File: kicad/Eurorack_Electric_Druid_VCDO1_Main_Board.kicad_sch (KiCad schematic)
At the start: 97 parts, among them J3 EuroPower_JST_3P, J4 EURO_PWR_16P, Q1 2N3904, U1 78M05, U2 79M05, U3 VCDO1, U4 TL074, U5 TL072, U6 TL074, U7 TL072

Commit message: updated schematic rev0.1.3
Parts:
- removed U7: TL072, DIYSynthMNL:DIP-8_W7.62mm_LongPads, symbol Amplifier_Operational:TL072
- added R51 (x4): 100K, DIYSynthMNL:R_quarter_watt_L6.3mm_D2.5mm_P7.62mm, symbol Device:R
- added U2: TL074, symbol Amplifier_Operational:TL074
- added unit 5 of U2
- added unit 4 of U2
- added unit 3 of U2
- added unit 2 of U2
- D16: value (none) -> ~
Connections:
- net +12V: now also U2.4 (V+)
- net +5V: now also Q1.3 (C); no longer R22.1
- net -12V: now also U2.11 (V-)
- net DIN_Glide_Input: now also Q1.1 (E), R22.1; no longer Q1.3 (C), R22.2
- net GND: now also R22.2, U2.10 (+), U2.12 (+), U2.3 (+), U2.5 (+); no longer Q1.1 (E)
- net at R50.2, R51.1, R53.2: now also U2.2 (-)
- net at R51.2: now also R51.1, U2.1; no longer R52.1
- net at R46.2, R47.1, R49.2: now also U2.9 (-)
- net at R48.1: now also R51.2, U2.14; no longer R47.2
- new net: R51.1, R51.2, U2.6 (-)
- new net: R51.2, R52.1, U2.7
- new net: R51.1, R51.2, U2.13 (-)
- new net: R47.2, R51.1, U2.8
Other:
- title: Eurorack Electric Druid VCDO1 - Main Board -> Eurorack Electric Druid VCDO1 - Control Board
- moved on the sheet: D13, D14, D15, D16, R21, R22, R46, R47, R48, R49, R52

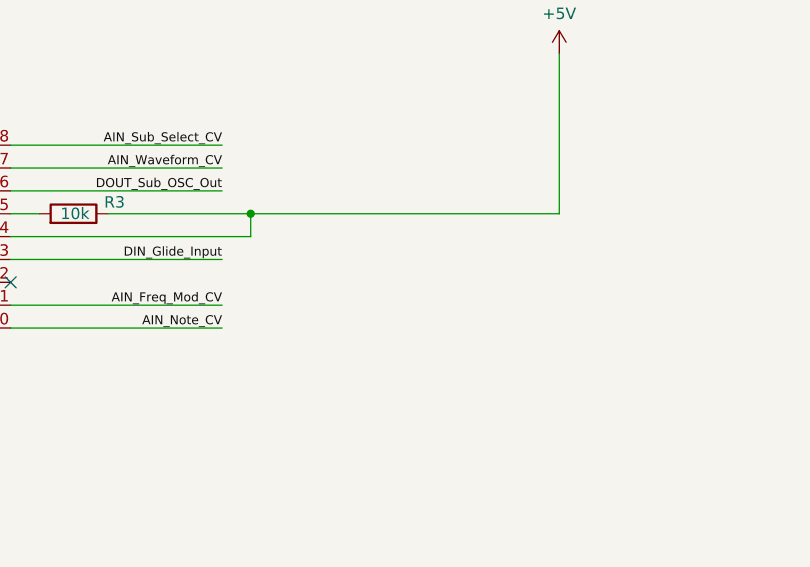
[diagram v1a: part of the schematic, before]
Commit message: Add 0.1.4 multiboard schematic
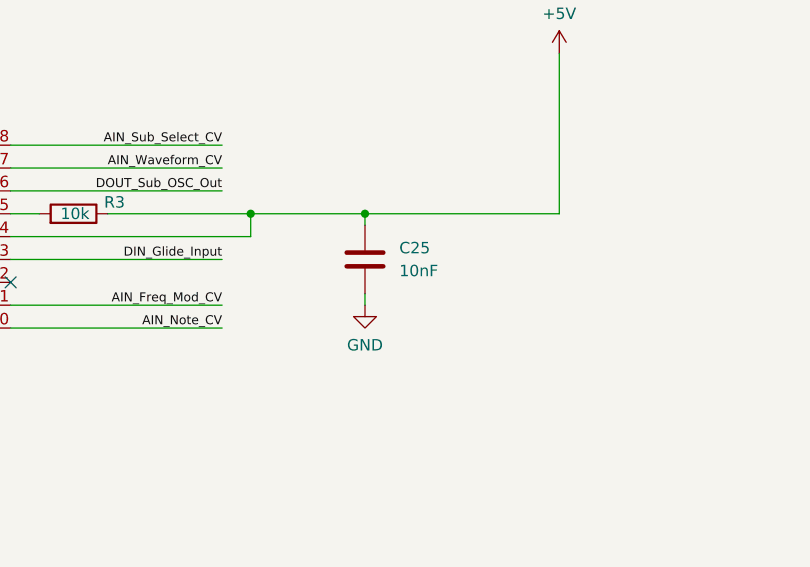
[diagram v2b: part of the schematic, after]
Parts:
- added C25: 10nF, symbol Device:C
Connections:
- net +5V: now also C25.1
- net GND: now also C25.2
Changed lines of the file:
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@@
     (title "Eurorack Electric Druid VCDO1 - Control Board")
     (date "2024-02-24")
-    (rev "0.1.3")
+    (rev "0.1.4")
     (company "DIYSynthMNL")
     (comment 1 "Shared under a CC BY-NC-SA 4.0 license. Some rights reserved.")
@@
   (junction (at 43.18 106.68) (diameter 0) (color 0 0 0 0)
   )
+  (junction (at 311.15 178.435) (diameter 0) (color 0 0 0 0)
+  )
   (junction (at 141.605 129.54) (diameter 0) (color 0 0 0 0)
   )
@@
     (stroke (width 0) (type default))
   )
+  (wire (pts (xy 311.15 188.595) (xy 311.15 187.325))
+    (stroke (width 0) (type default))
+  )
   (wire (pts (xy 60.96 62.865) (xy 60.96 71.755))
     (stroke (width 0) (type default))
@@
     (stroke (width 0) (type default))
   )
+  (wire (pts (xy 311.15 179.705) (xy 311.15 178.435))
+    (stroke (width 0) (type default))
+  )
   (wire (pts (xy 290.195 90.805) (xy 290.195 98.425))
     (stroke (width 0) (type default))
@@
     (stroke (width 0) (type default))
   )
-  (wire (pts (xy 332.74 178.435) (xy 298.45 178.435))
+  (wire (pts (xy 332.74 178.435) (xy 311.15 178.435))
     (stroke (width 0) (type default))
   )
@@
     (stroke (width 0) (type default))
   )
+  (wire (pts (xy 311.15 178.435) (xy 298.45 178.435))
+    (stroke (width 0) (type default))
+  )
   (wire (pts (xy 372.745 41.275) (xy 370.84 41.275))
     (stroke (width 0) (type default))
@@
     )
   )
+  (symbol (lib_id "power:GND") (at 311.15 188.595 0) (unit 1)
+    (in_bom yes) (on_board yes) (dnp no) (fields_autoplaced)
+    (property "Reference" "#PWR050" (at 311.15 194.945 0)
+      (effects (font (size 1.27 1.27)) hide)
+    )
+    (property "Value" "GND" (at 311.15 193.04 0)
+      (effects (font (size 1.27 1.27)))
+    )
+    (property "Footprint" "" (at 311.15 188.595 0)
+      (effects (font (size 1.27 1.27)) hide)
+    )
+    (property "Datasheet" "" (at 311.15 188.595 0)
+      (effects (font (size 1.27 1.27)) hide)
+    )
+    (pin "1")
+    (instances
+      (project "Electric Druid VCDO1"
+        (path "/1a79e409-2950-446e-9b6e-16f6bf0a888d/940513db-8445-4e70-8397-130f22045b59"
+          (reference "#PWR050") (unit 1)
+        )
+      )
+    )
+  )
   (symbol (lib_id "Device:R") (at 135.89 68.58 90) (unit 1)
     (in_bom yes) (on_board yes) (dnp no) (fields_autoplaced)
@@
         )
       )
+    )
+  )
+  (symbol (lib_id "Device:C") (at 311.15 183.515 0) (unit 1)
+    (in_bom yes) (on_board yes) (dnp no)
+    (property "Reference" "C25" (at 314.96 182.245 0)
+      (effects (font (size 1.27 1.27)) (justify left))
+    )
+    (property "Value" "10nF" (at 314.96 184.785 0)
+      (effects (font (size 1.27 1.27)) (justify left))
+    )
+    (property "Footprint" "" (at 312.1152 187.325 0)
+      (effects (font (size 1.27 1.27)) hide)
+    )
+    (property "Datasheet" "~" (at 311.15 183.515 0)
+      (effects (font (size 1.27 1.27)) hide)
+    )
+    (pin "2")
+    (pin "1")
+    (instances
+      (project "Electric Druid VCDO1"
+        (path "/1a79e409-2950-446e-9b6e-16f6bf0a888d/940513db-8445-4e70-8397-130f22045b59"
+          (reference "C25") (unit 1)
+        )
+      )

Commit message: Add schematic rev 0.1.5
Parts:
- added C26: 100nF, symbol Device:C
- C25: value 10nF -> 100nF
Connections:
- net AIN_Note_CV: now also C26.1
- net GND: now also C26.2
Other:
- note added: "4K7 resistors protect ADC against overvoltage"
- note added: "Modifications added to datasheet circuit: - Bitcrush and Glide CV input circuits - Input protection diodes on Glide on/off cv - Note CV noise filter cap"
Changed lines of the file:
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@@
     (title "Eurorack Electric Druid VCDO1 - Control Board")
     (date "2024-02-24")
-    (rev "0.1.4")
+    (rev "0.1.5")
     (company "DIYSynthMNL")
     (comment 1 "Shared under a CC BY-NC-SA 4.0 license. Some rights reserved.")
+    (comment 2 "All credits go to Tom Wiltshire, founder of Electric Druid")
+    (comment 3 "Redrawn and Modified by Neo Recasata (DIYSynthMNL)")
   )
   (junction (at 129.54 123.825) (diameter 0) (color 0 0 0 0)
@@
   (junction (at 133.35 238.125) (diameter 0) (color 0 0 0 0)
   )
+  (junction (at 275.59 191.135) (diameter 0) (color 0 0 0 0)
+  )
   (junction (at 144.145 265.43) (diameter 0) (color 0 0 0 0)
   )
@@
     (stroke (width 0) (type default))
   )
+  (wire (pts (xy 275.59 191.135) (xy 295.275 191.135))
+    (stroke (width 0) (type default))
+  )
   (wire (pts (xy 51.435 274.32) (xy 51.435 271.145))
     (stroke (width 0) (type default))
@@
     (stroke (width 0) (type default))
   )
-  (wire (pts (xy 271.78 191.135) (xy 295.275 191.135))
+  (wire (pts (xy 271.78 191.135) (xy 275.59 191.135))
     (stroke (width 0) (type default))
   )
@@
     (stroke (width 0) (type default))
   )
+  (wire (pts (xy 275.59 199.39) (xy 275.59 200.66))
+    (stroke (width 0) (type default))
+  )
   (wire (pts (xy 103.505 265.43) (xy 106.68 265.43))
     (stroke (width 0) (type default))
@@
     (stroke (width 0) (type default))
   )
+  (wire (pts (xy 275.59 191.77) (xy 275.59 191.135))
+    (stroke (width 0) (type default))
+  )
   (wire (pts (xy 48.895 32.385) (xy 48.895 30.48))
     (stroke (width 0) (type default))
@@
     (fill (type none))
   )
-  (image (at 312.42 259.08) (scale 0.336315)
+  (image (at 396.24 257.81) (scale 0.336315)
     (data
       iVBORw0KGgoAAAANSUhEUgAAAwAAAAENCAYAAAC4gAJ5AAAABHNCSVQICAgIfAhkiAAAIABJREFU
@@
     (effects (font (size 1.27 1.27)) (justify left bottom))
   )
+  (text "Modifications added to datasheet circuit:\n- Bitcrush and Glide CV input circuits\n- Input protection diodes on Glide on/off cv\n- Note CV noise filter cap\n"
+    (at 300.99 231.775 0)
+    (effects (font (size 1.27 1.27)) (justify left bottom))
+  )
   (text "*Optional Load Resistor" (at 95.885 279.4 0)
     (effects (font (size 1.27 1.27)) (justify left bottom))
@@
     (effects (font (size 1.27 1.27)) (justify left bottom))
   )
+  (text "4K7 resistors protect ADC against overvoltage" (at 44.45 172.085 0)
+    (effects (font (size 1.27 1.27)) (justify left bottom))
+  )
   (text "CV=Jacks\nControl=Pots" (at 236.22 196.85 0)
     (effects (font (size 1.27 1.27)) (justify left bottom))
@@
     )
   )
+  (symbol (lib_id "power:GND") (at 275.59 200.66 0) (unit 1)
+    (in_bom yes) (on_board yes) (dnp no) (fields_autoplaced)
+    (property "Reference" "#PWR051" (at 275.59 207.01 0)
+      (effects (font (size 1.27 1.27)) hide)
+    )
+    (property "Value" "GND" (at 275.59 205.105 0)
+      (effects (font (size 1.27 1.27)))
+    )
+    (property "Footprint" "" (at 275.59 200.66 0)
+      (effects (font (size 1.27 1.27)) hide)
+    )
+    (property "Datasheet" "" (at 275.59 200.66 0)
+      (effects (font (size 1.27 1.27)) hide)
+    )
+    (pin "1")
+    (instances
+      (project "Electric Druid VCDO1"
+        (path "/1a79e409-2950-446e-9b6e-16f6bf0a888d/940513db-8445-4e70-8397-130f22045b59"
+          (reference "#PWR051") (unit 1)
+        )
+      )
+    )
+  )
   (symbol (lib_id "Device:R") (at 135.89 68.58 90) (unit 1)
     (in_bom yes) (on_board yes) (dnp no) (fields_autoplaced)
@@
     )
   )
+  (symbol (lib_id "Device:C") (at 275.59 195.58 0) (unit 1)
+    (in_bom yes) (on_board yes) (dnp no)
+    (property "Reference" "C26" (at 279.4 194.31 0)
+      (effects (font (size 1.27 1.27)) (justify left))
+    )
+    (property "Value" "100nF" (at 279.4 196.85 0)
+      (effects (font (size 1.27 1.27)) (justify left))
+    )
+    (property "Footprint" "" (at 276.5552 199.39 0)
+      (effects (font (size 1.27 1.27)) hide)
+    )
+    (property "Datasheet" "~" (at 275.59 195.58 0)
+      (effects (font (size 1.27 1.27)) hide)
+    )
+    (pin "2")
+    (pin "1")
+    (instances
+      (project "Electric Druid VCDO1"
+        (path "/1a79e409-2950-446e-9b6e-16f6bf0a888d/940513db-8445-4e70-8397-130f22045b59"
+          (reference "C26") (unit 1)
+        )
+      )
+    )
+  )
   (symbol (lib_id "Amplifier_Operational:TL074") (at 52.07 109.22 0) (mirror x) (unit 3)
     (in_bom yes) (on_board yes) (dnp no)
@@
       (effects (font (size 1.27 1.27)) (justify left))
     )
-    (property "Value" "10nF" (at 314.96 184.785 0)
+    (property "Value" "100nF" (at 314.96 184.785 0)
       (effects (font (size 1.27 1.27)) (justify left))
     )
